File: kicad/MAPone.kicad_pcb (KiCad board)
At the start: 2 copper layers, 95 x 30 mm, 49 parts, among them J1 BARREL_JACK, J2 USB-Micro, J3 USB-Micro, P1 CONN_1, P2 CONN_1, P3 CONN_1, P4 CONN_1, P5 CONN_1, P6 CONN_1, SW1 RST, U1 7805, U2 ATMEGA328-P, U3 CP210X, X1 16MHz

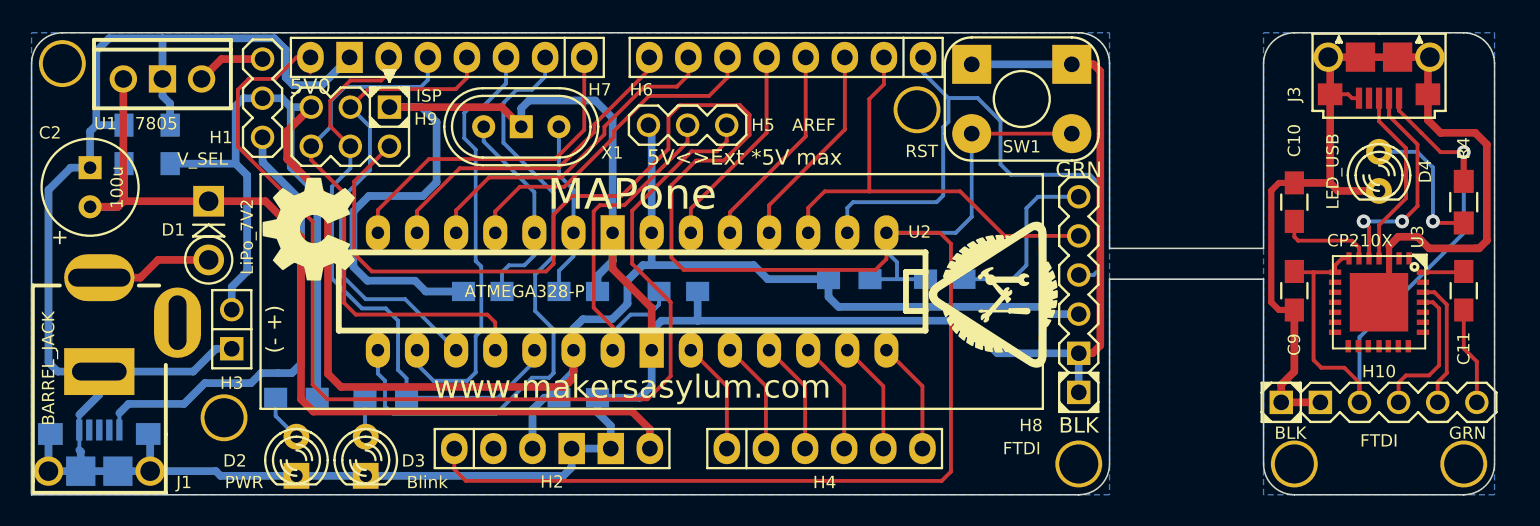
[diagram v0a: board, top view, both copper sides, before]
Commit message: MAPone changed header locations to fit Breadboard instead of Arduino
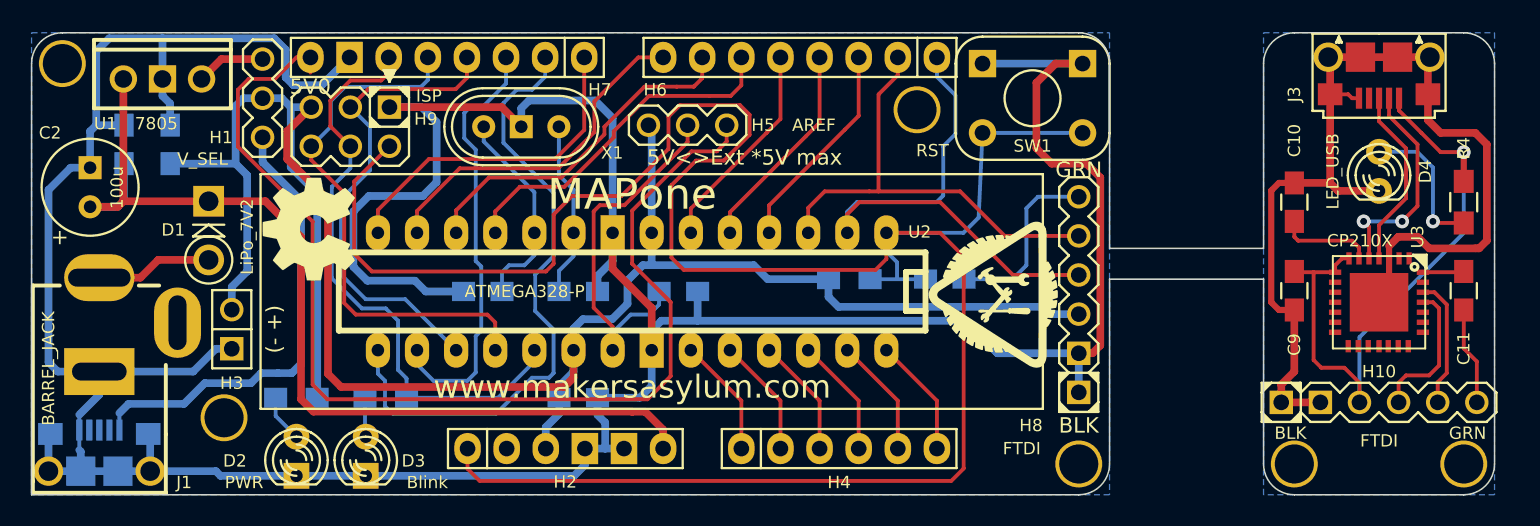
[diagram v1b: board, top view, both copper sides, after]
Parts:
- moved H4 0.94 mm to (82.4, 57.0)
- moved H6 0.90 mm to (79.9, 31.6)
- moved H2 0.86 mm to (64.7, 57.0)
- moved SW1 0.70 mm to (95.0, 34.2)
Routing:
- net GND: track 321.0 -> 325.4 mm
- net /PD7: track 22.3 -> 24.4 mm
- net /RXD: track 38.8 -> 37.3 mm
- net /PD5_P: track 22.6 -> 23.8 mm
- net /PD6_P: track 21.6 -> 22.6 mm
- net /5V: track 137.7 -> 136.8 mm
- net /V_IN: track 62.8 -> 63.6 mm
- net /RST: track 148.8 -> 149.5 mm

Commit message: MAPone realigned headers to fit 0.1 breadboard
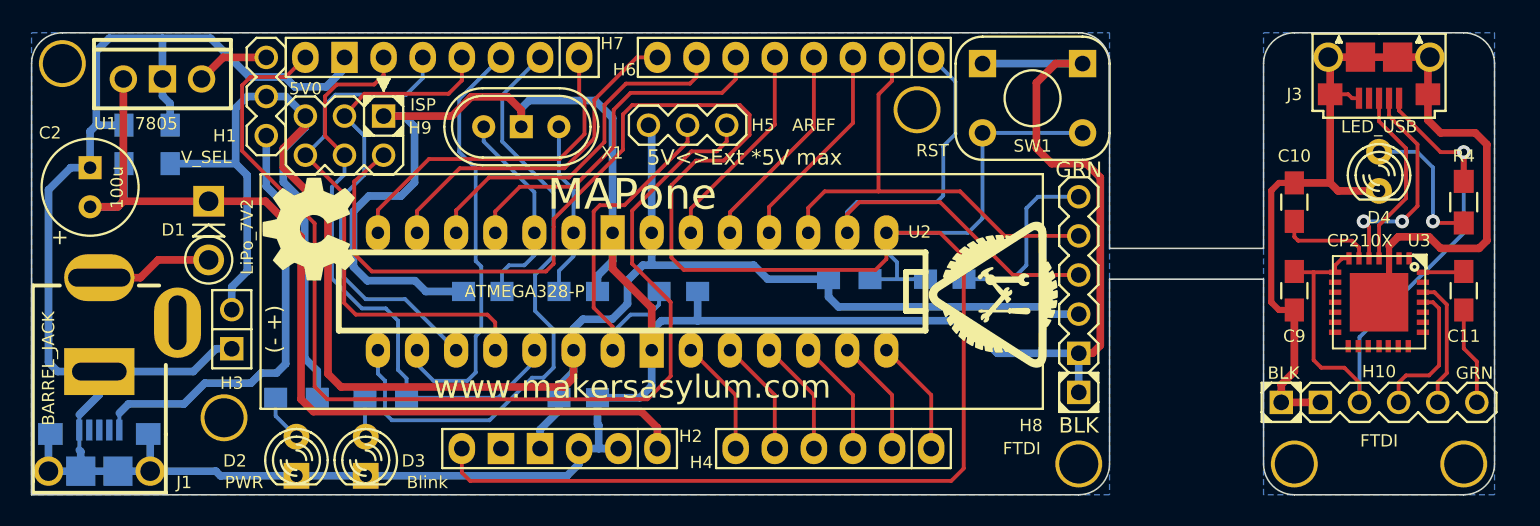
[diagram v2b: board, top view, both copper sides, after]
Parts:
- Z1: footprint MAPone.pretty:MA_Logo -> MAPone.pretty:MA_Logo2
- moved H9 0.69 mm to (50.3, 36.7)
- moved H4 0.37 mm to (82.1, 57.0), turned to 0 degrees
- moved H6 0.37 mm to (79.5, 31.6)
- moved H2 0.37 mm to (64.3, 57.0), turned to 0 degrees
- moved H7 0.33 mm to (56.7, 31.6)
- moved H1 0.26 mm to (45.2, 34.1)
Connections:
- C10 pad 2: GND -> /USB_UART/GND_U
- C9 pad 2: GND -> /USB_UART/GND_U
- D4 pad 2: GND -> /USB_UART/GND_U
- H10 pad 1: GND -> /USB_UART/GND_U
- H10 pad 2: GND -> /USB_UART/GND_U
- H2 pad 1: /RST -> /V_IN
- H2 pad 2: /3V3 -> GND
- H2 pad 3: /5V -> GND
- H2 pad 4: GND -> /5V
- H2 pad 5: GND -> (no net)
- H2 pad 6: /V_IN -> /RST
- H4 pad 1: /AD0 -> /AD5_SCL
- H4 pad 2: /AD1 -> /AD4_SDA
- H4 pad 3: /AD2 -> /AD3
- H4 pad 4: /AD3 -> /AD2
- H4 pad 5: /AD4_SDA -> /AD1
- H4 pad 6: /AD5_SCL -> /AD0
- J1 pad 3: Net-(J1-Pad3) -> (no net)
- J2 pad 2: Net-(J2-Pad2) -> (no net)
- J2 pad 3: Net-(J2-Pad3) -> (no net)
- J2 pad 4: Net-(J2-Pad4) -> (no net)
- J3 pad 4: Net-(J3-Pad4) -> (no net)
- J3 pad 5: GND -> /USB_UART/GND_U
- J3 pad T1: GND -> /USB_UART/GND_U
- J3 pad T2: GND -> /USB_UART/GND_U
- J3 pad T3: GND -> /USB_UART/GND_U
- J3 pad T4: GND -> /USB_UART/GND_U
- J3 pad T5: GND -> /USB_UART/GND_U
- J3 pad T6: GND -> /USB_UART/GND_U
- P1 pad 1: Net-(P1-Pad1) -> (no net)
- P2 pad 1: Net-(P2-Pad1) -> (no net)
- P3 pad 1: Net-(P3-Pad1) -> (no net)
- P4 pad 1: Net-(P4-Pad1) -> (no net)
- P5 pad 1: Net-(P5-Pad1) -> (no net)
- P6 pad 1: Net-(P6-Pad1) -> (no net)
- U3 pad 1: Net-(U3-Pad1) -> (no net)
- U3 pad 11: Net-(U3-Pad11) -> (no net)
- U3 pad 12: Net-(U3-Pad12) -> (no net)
- U3 pad 2: Net-(U3-Pad2) -> (no net)
- U3 pad 23: /USB_UART/CTS -> (no net)
- U3 pad 24: /USB_UART/RTS -> (no net)
- U3 pad 27: Net-(U3-Pad27) -> (no net)
- U3 pad 29: GND -> /USB_UART/GND_U
- U3 pad 3: GND -> /USB_UART/GND_U
- U3 pad 9: Net-(U3-Pad9) -> (no net)
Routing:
- net GND: track 325.4 -> 250.3 mm
- net /USB_UART/GND_U: track 0.00 -> 72.6 mm
- net /Vext: track 72.8 -> 71.3 mm
- net /V_USB: track 30.0 -> 28.6 mm
- net /PD7: track 24.4 -> 23.3 mm
- net /RXD: track 37.3 -> 36.5 mm
- net /USB_UART/5V: track 42.6 -> 41.8 mm
- net /PD6_P: track 22.6 -> 23.3 mm
- net /PD5_P: track 23.8 -> 24.4 mm
- added copper zone on B.Cu, net /USB_UART/GND_U
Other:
- board text added: "* disable when using ISP/FTDI"
- board text added: "D8:D9:D10:D11:D12:D13:Gnd:Vext"
- board text removed: "* disable when using H8 or H9"
- board text removed: "D0:D1:D2:D3:D4:D5:D6:D7:Gnd:Vext"

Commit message: MAPone made MAPusart smaller
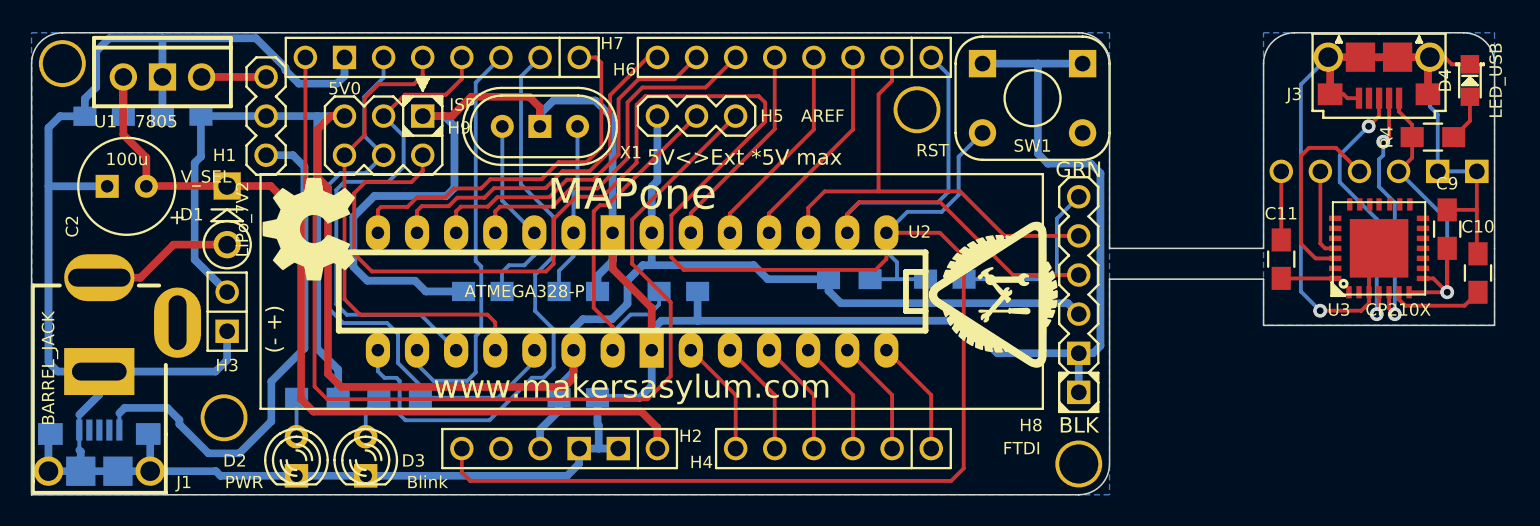
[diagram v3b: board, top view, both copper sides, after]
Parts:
- removed P5, P6: CONN_1, MAPone.pretty:vite_3mm
- D4: footprint MAPone.pretty:LED-3MM -> MAPone.pretty:LED-0805
- H10: footprint MAPone.pretty:Header_FTDI -> MAPone.pretty:Socket_Strip_Angled_1x06; moved to B.Cu
- moved H10 15.0 mm to (117.5, 39.0)
- moved C10 12.8 mm to (123.9, 45.6)
- moved C11 12.0 mm to (111.2, 44.7), turned to 90 degrees
- moved C9 10.7 mm to (121.9, 42.8), turned to 90 degrees
- moved D4 8.34 mm to (123.4, 33.1), turned to 90 degrees
- moved R4 4.67 mm to (121.0, 36.8), turned to 0 degrees
- moved C2 3.88 mm to (37.5, 40.0), turned to 180 degrees
- moved U3 3.50 mm to (117.5, 44.0), turned to 0 degrees
- moved Z3 3.00 mm to (117.5, 45.0)
- moved H9 2.54 mm to (52.9, 36.7)
- moved C3 2.24 mm to (34.7, 35.4), turned to 0 degrees
- moved C4 1.99 mm to (39.8, 35.4), turned to 180 degrees
- moved D1 1.56 mm to (42.7, 41.8)
- moved R2 1.36 mm to (48.6, 53.7)
- moved H1 1.27 mm to (45.2, 35.4)
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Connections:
- H10 pad 4: /USB_UART/RXD -> /USB_UART/TXD
- H10 pad 5: /USB_UART/TXD -> /USB_UART/RXD
- H2 pad 5: (no net) -> /3V3
- J1 pad 3: (no net) -> Net-(J1-Pad3)
- J2 pad 2: (no net) -> Net-(J2-Pad2)
- J2 pad 3: (no net) -> Net-(J2-Pad3)
- J2 pad 4: (no net) -> Net-(J2-Pad4)
- J3 pad 4: (no net) -> Net-(J3-Pad4)
- P1 pad 1: (no net) -> Net-(P1-Pad1)
- P2 pad 1: (no net) -> Net-(P2-Pad1)
- P3 pad 1: (no net) -> Net-(P3-Pad1)
- P4 pad 1: (no net) -> Net-(P4-Pad1)
- U3 pad 1: (no net) -> Net-(U3-Pad1)
- U3 pad 11: (no net) -> Net-(U3-Pad11)
- U3 pad 12: (no net) -> Net-(U3-Pad12)
- U3 pad 2: (no net) -> Net-(U3-Pad2)
- U3 pad 23: (no net) -> Net-(U3-Pad23)
- U3 pad 24: (no net) -> Net-(U3-Pad24)
- U3 pad 27: (no net) -> Net-(U3-Pad27)
- U3 pad 9: (no net) -> Net-(U3-Pad9)
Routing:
- net /USB_UART/5V: track 41.8 -> 21.9 mm
- net /USB_UART/GND_U: track 72.6 -> 63.3 mm, vias 0 -> 1
- net Net-(D4-Pad1): track 9.46 -> 3.06 mm, vias 1 -> 0
- net /USB_UART/D+: track 11.8 -> 17.6 mm, vias 0 -> 2
- net /V_IN: track 63.3 -> 58.3 mm
- net /V_USB: track 28.6 -> 33.6 mm
- net /Vext: track 71.3 -> 66.4 mm
- net /USB_UART/TXD: track 8.48 -> 13.0 mm
- net /MISO: track 35.0 -> 31.4 mm
- net /USB_UART/RXD: track 9.28 -> 5.78 mm
- net /RST: track 149.6 -> 146.5 mm
- net /PB0: track 22.1 -> 24.7 mm
- net /5V: track 136.5 -> 134.1 mm
- net /USB_UART/D-: track 14.2 -> 16.3 mm
- net Net-(C11-Pad2): track 6.35 -> 4.45 mm
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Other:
- outline, holes or cut-outs redrawn

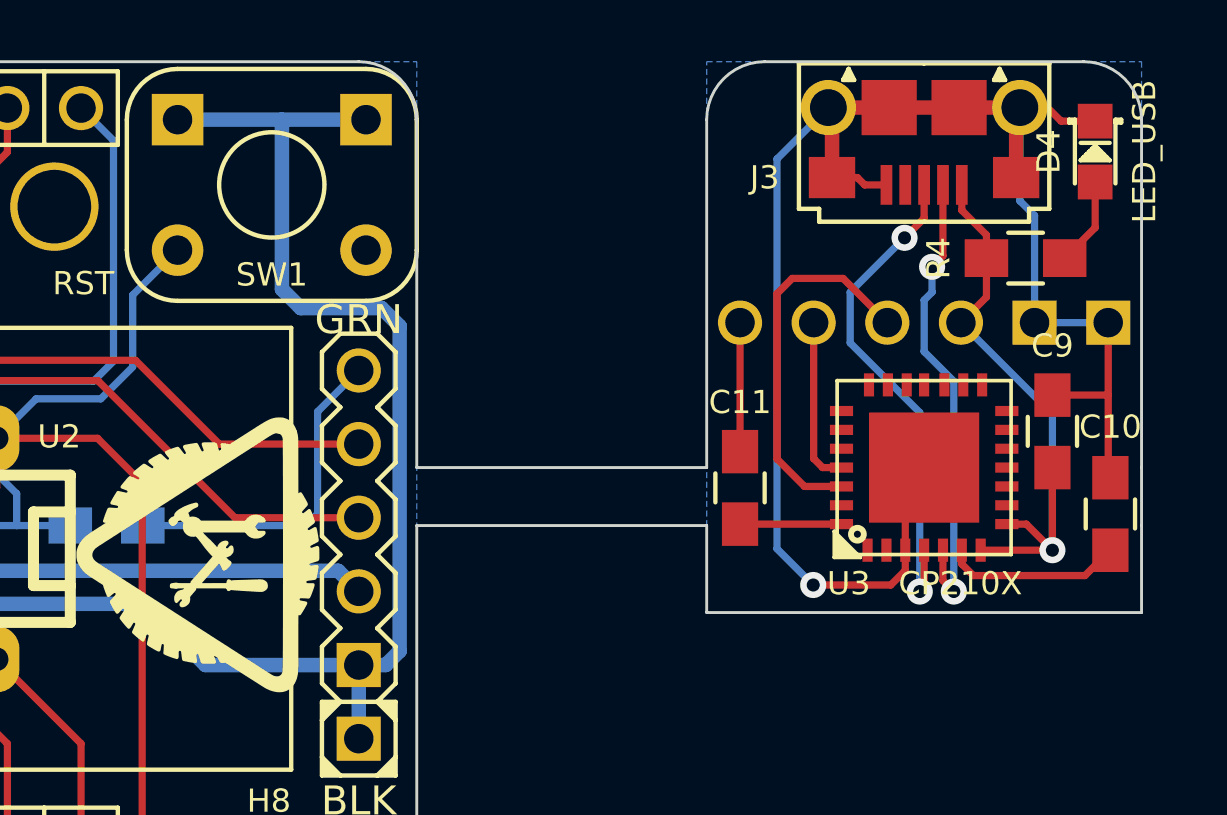
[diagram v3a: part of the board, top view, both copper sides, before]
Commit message: MAPone made MAPusart smaller
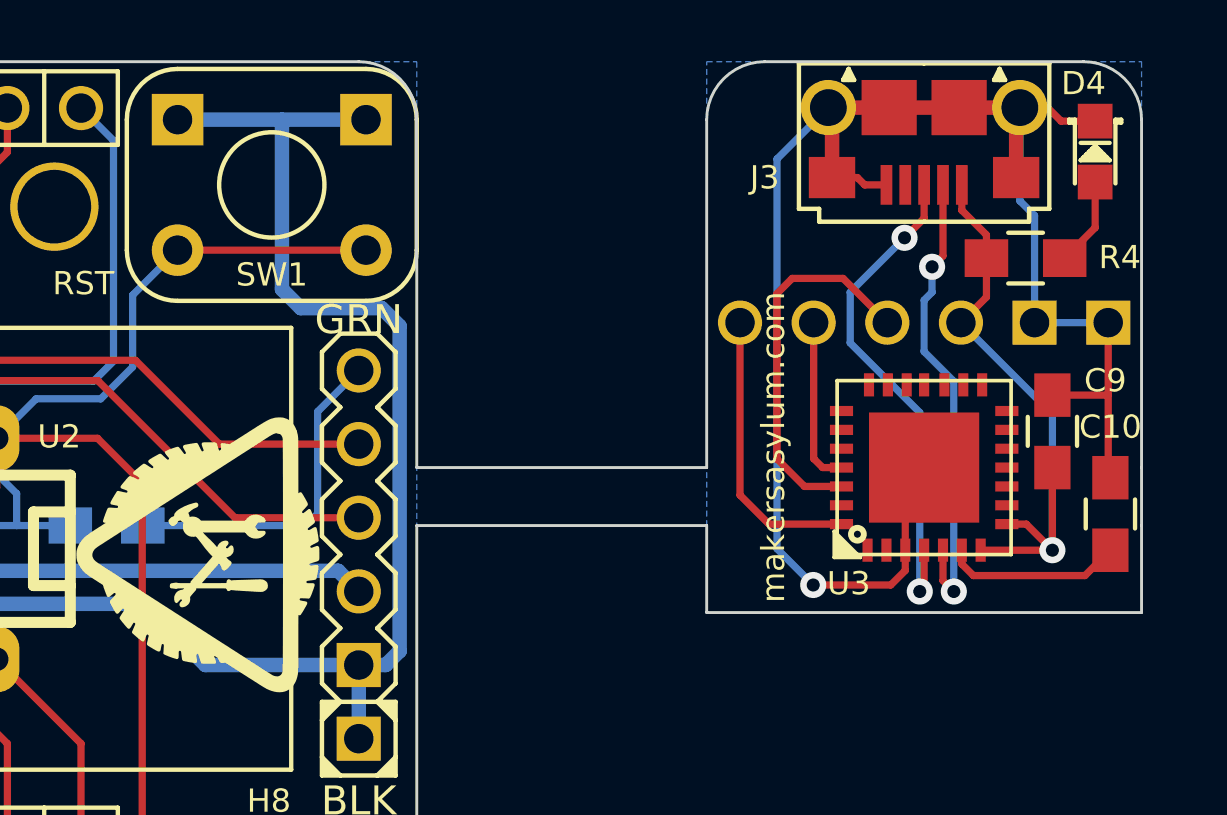
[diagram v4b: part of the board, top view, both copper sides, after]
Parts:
- removed C11: 100n, MAPone.pretty:C_0805_HandSoldering
- moved Z5 0.50 mm to (117.5, 34.0)
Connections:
- H10 pad 6: Net-(C11-Pad2) -> /USB_UART/RST
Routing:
- net /RST: track 146.5 -> 153.0 mm
- net /USB_UART/RST: track 3.50 -> 9.87 mm
- net Net-(C11-Pad2): track 4.45 -> 0.00 mm
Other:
- board text added: "BLK"
- board text added: "GRN"
- board text added: "makersasylum.com"

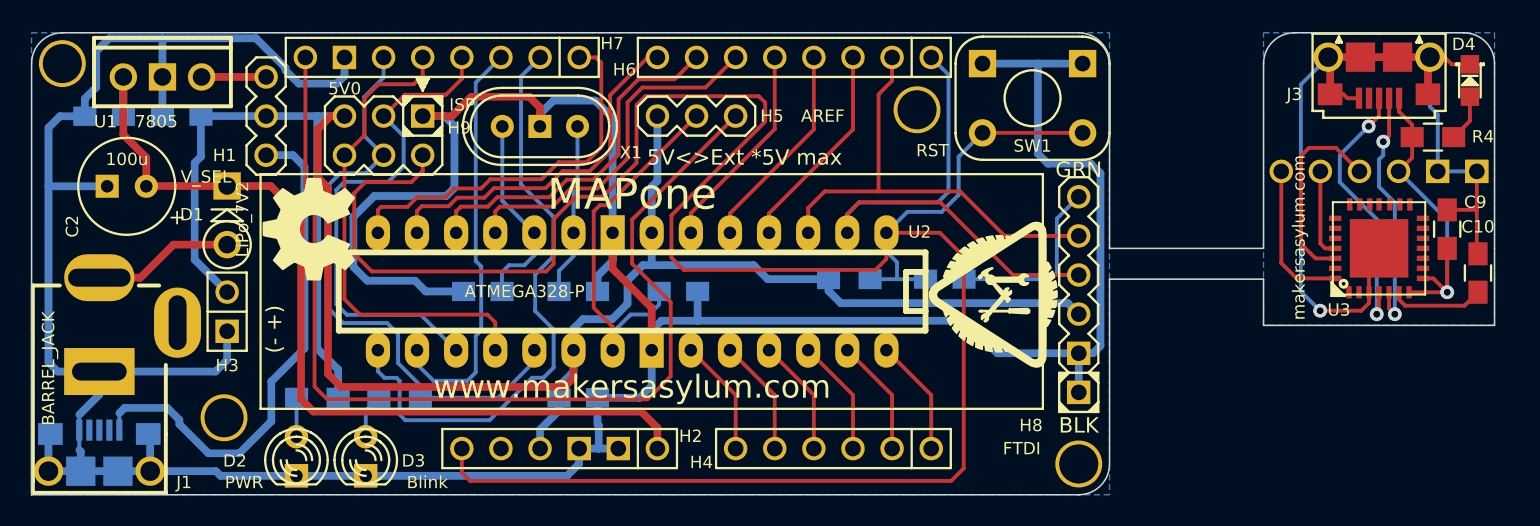
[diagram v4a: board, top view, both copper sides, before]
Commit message: MAPone hived off USB<>UART bridge to separate project MAPusart
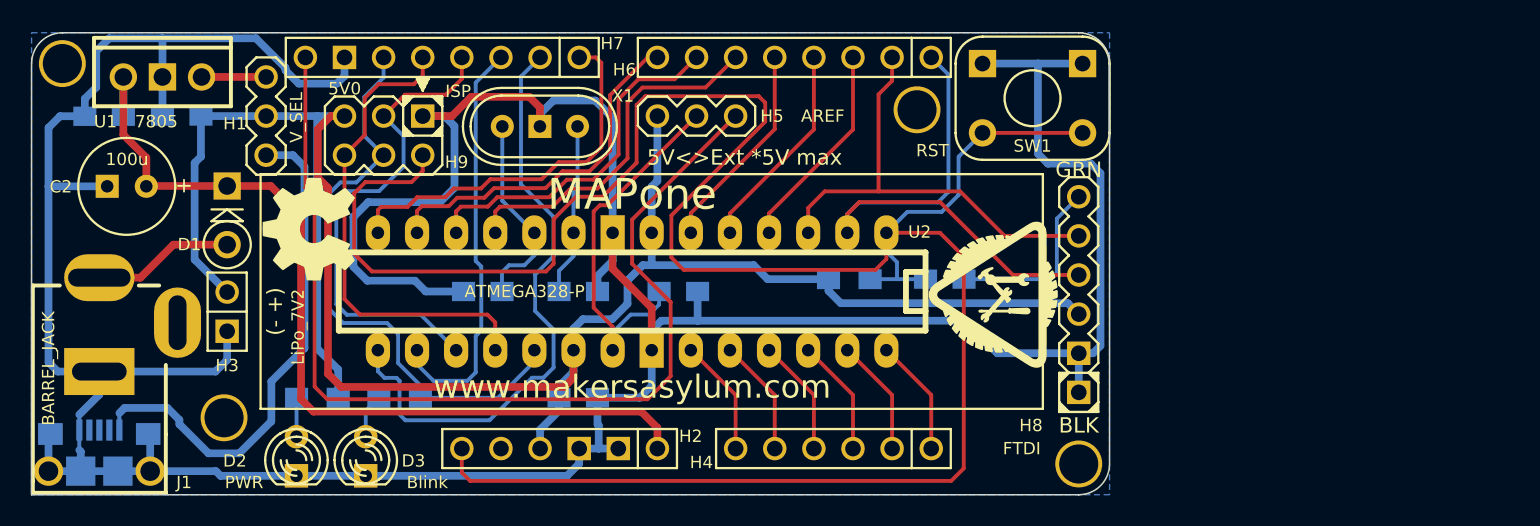
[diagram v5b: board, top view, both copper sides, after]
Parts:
- removed C10, C9: 100n, MAPone.pretty:C_0805_HandSoldering
- removed D4: LED_USB, MAPone.pretty:LED-0805
- removed H10: FTDI, MAPone.pretty:Socket_Strip_Angled_1x06
- removed J3: USB-Micro, MAPone.pretty:USB_B_Micro
- removed R4: 300E, MAPone.pretty:R_0805_HandSoldering
- removed U3: CP210X, MAPone.pretty:qfn-28
- removed Z3: CONN_1, MAPone.pretty:MA_Logo2
- removed Z5: CONN_1, MAPone:OSHW_6mm
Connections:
- H2 pad 5: /3V3 -> (no net)
- J1 pad 3: Net-(J1-Pad3) -> (no net)
- J2 pad 2: Net-(J2-Pad2) -> (no net)
- J2 pad 3: Net-(J2-Pad3) -> (no net)
- J2 pad 4: Net-(J2-Pad4) -> (no net)
- P1 pad 1: Net-(P1-Pad1) -> (no net)
- P2 pad 1: Net-(P2-Pad1) -> (no net)
- P3 pad 1: Net-(P3-Pad1) -> (no net)
- P4 pad 1: Net-(P4-Pad1) -> (no net)
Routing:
- net /USB_UART/GND_U: track 63.3 -> 0.00 mm, vias 1 -> 0
- net /USB_UART/5V: track 21.9 -> 0.00 mm, vias 1 -> 0
- net /USB_UART/D+: track 17.6 -> 0.00 mm, vias 2 -> 0
- net /USB_UART/D-: track 16.3 -> 0.00 mm, vias 2 -> 0
- net /USB_UART/TXD: track 13.0 -> 0.00 mm
- net /USB_UART/RST: track 9.87 -> 0.00 mm
- net /USB_UART/3V3: track 6.13 -> 0.00 mm
- net /USB_UART/RXD: track 5.78 -> 0.00 mm
- net Net-(D4-Pad1): track 3.06 -> 0.00 mm
- removed copper zone on B.Cu, net /USB_UART/GND_U
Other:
- board size 95 x 30 mm -> 70 x 30 mm
- board text added: "(-+)"
- board text removed: "BLK"
- board text removed: "GRN"
- board text removed: "MAPusart"
- board text removed: "makersasylum.com"
